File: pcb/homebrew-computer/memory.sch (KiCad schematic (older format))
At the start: 3 parts

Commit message: Add clock generation
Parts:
- removed U? (x2): SN74AVC8T245RHLR, symbol 74AVC8T245:SN74AVC8T245RHLR
- added U? (x3): SN74AVC16T245DGGR, symbol 74AVC16T245:SN74AVC16T245DGGR
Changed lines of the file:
@@
 $Descr User 9843 8268
 encoding utf-8
-Sheet 6 7
+Sheet 6 8
 Title ""
 Date ""
@@
 $EndComp
 $Comp
-L 74AVC8T245:SN74AVC8T245RHLR U?
-U 1 1 5F979582
-P 2400 1400
-F 0 "U?" H 2400 1181 50  0000 C CNN
-F 1 "SN74AVC8T245RHLR" H 2400 1090 50  0000 C CNN
-F 2 "" H 2400 1400 50  0001 C CNN
-F 3 "" H 2400 1400 50  0001 C CNN
-	1    2400 1400
+L 74AVC16T245:SN74AVC16T245DGGR U?
+U 1 1 5F907EBD
+P 2550 2800
+F 0 "U?" H 2500 2865 50  0000 C CNN
+F 1 "SN74AVC16T245DGGR" H 2500 2774 50  0000 C CNN
+F 2 "" H 2550 2800 50  0001 C CNN
+F 3 "" H 2550 2800 50  0001 C CNN
+	1    2550 2800
 	1    0    0    -1
 $EndComp
 $Comp
-L 74AVC8T245:SN74AVC8T245RHLR U?
-U 1 1 5F97A12B
-P 2400 3350
-F 0 "U?" H 2400 3131 50  0000 C CNN
-F 1 "SN74AVC8T245RHLR" H 2400 3040 50  0000 C CNN
-F 2 "" H 2400 3350 50  0001 C CNN
-F 3 "" H 2400 3350 50  0001 C CNN
-	1    2400 3350
+L 74AVC16T245:SN74AVC16T245DGGR U?
+U 2 1 5F908C70
+P 2500 3650
+F 0 "U?" H 2525 3665 50  0000 C CNN
+F 1 "SN74AVC16T245DGGR" H 2525 3574 50  0000 C CNN
+F 2 "" H 2500 3650 50  0001 C CNN
+F 3 "" H 2500 3650 50  0001 C CNN
+	2    2500 3650
 	1    0    0    -1
 $EndComp
+$Comp
+L 74AVC16T245:SN74AVC16T245DGGR U?
+U 3 1 5F909A93
+P 2550 5100
+F 0 "U?" H 2625 5115 50  0000 C CNN
+F 1 "SN74AVC16T245DGGR" H 2625 5024 50  0000 C CNN
+F 2 "" H 2550 5100 50  0001 C CNN
+F 3 "" H 2550 5100 50  0001 C CNN
+	3    2550 5100
+	1    0    0    -1
+$EndComp

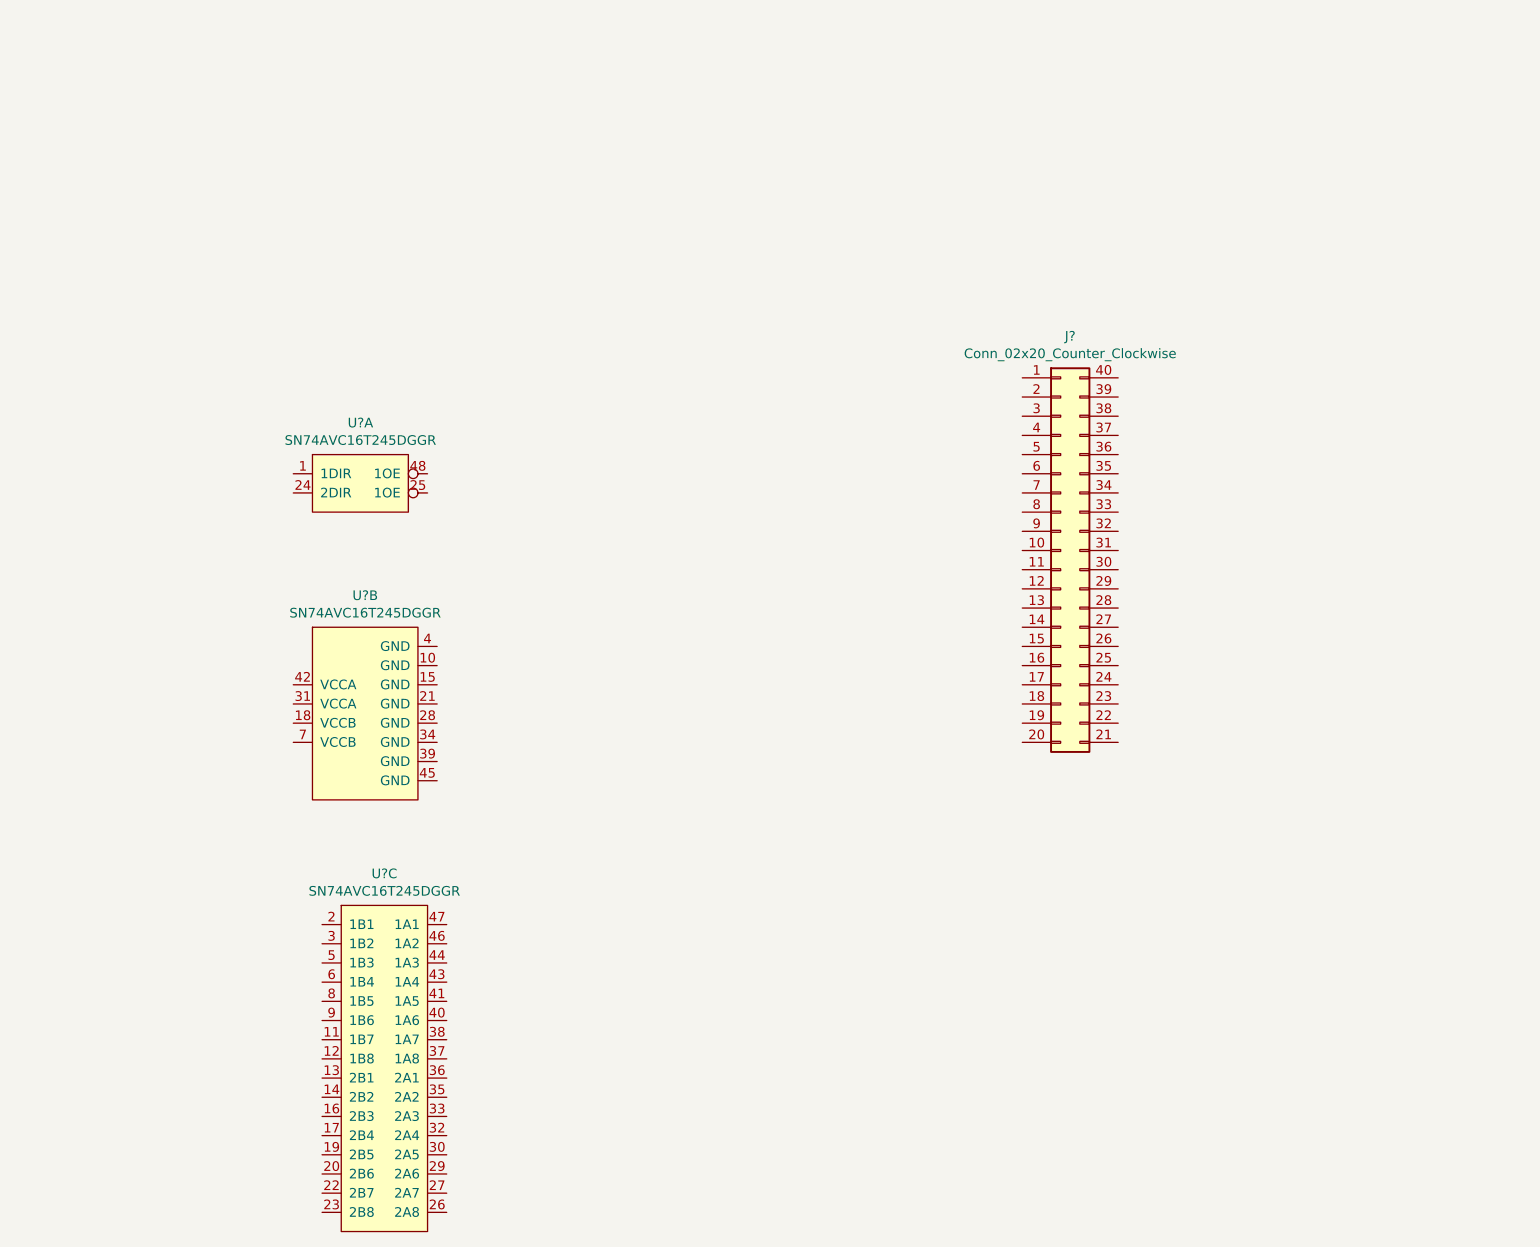
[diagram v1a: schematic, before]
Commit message: Add the memory interface logic
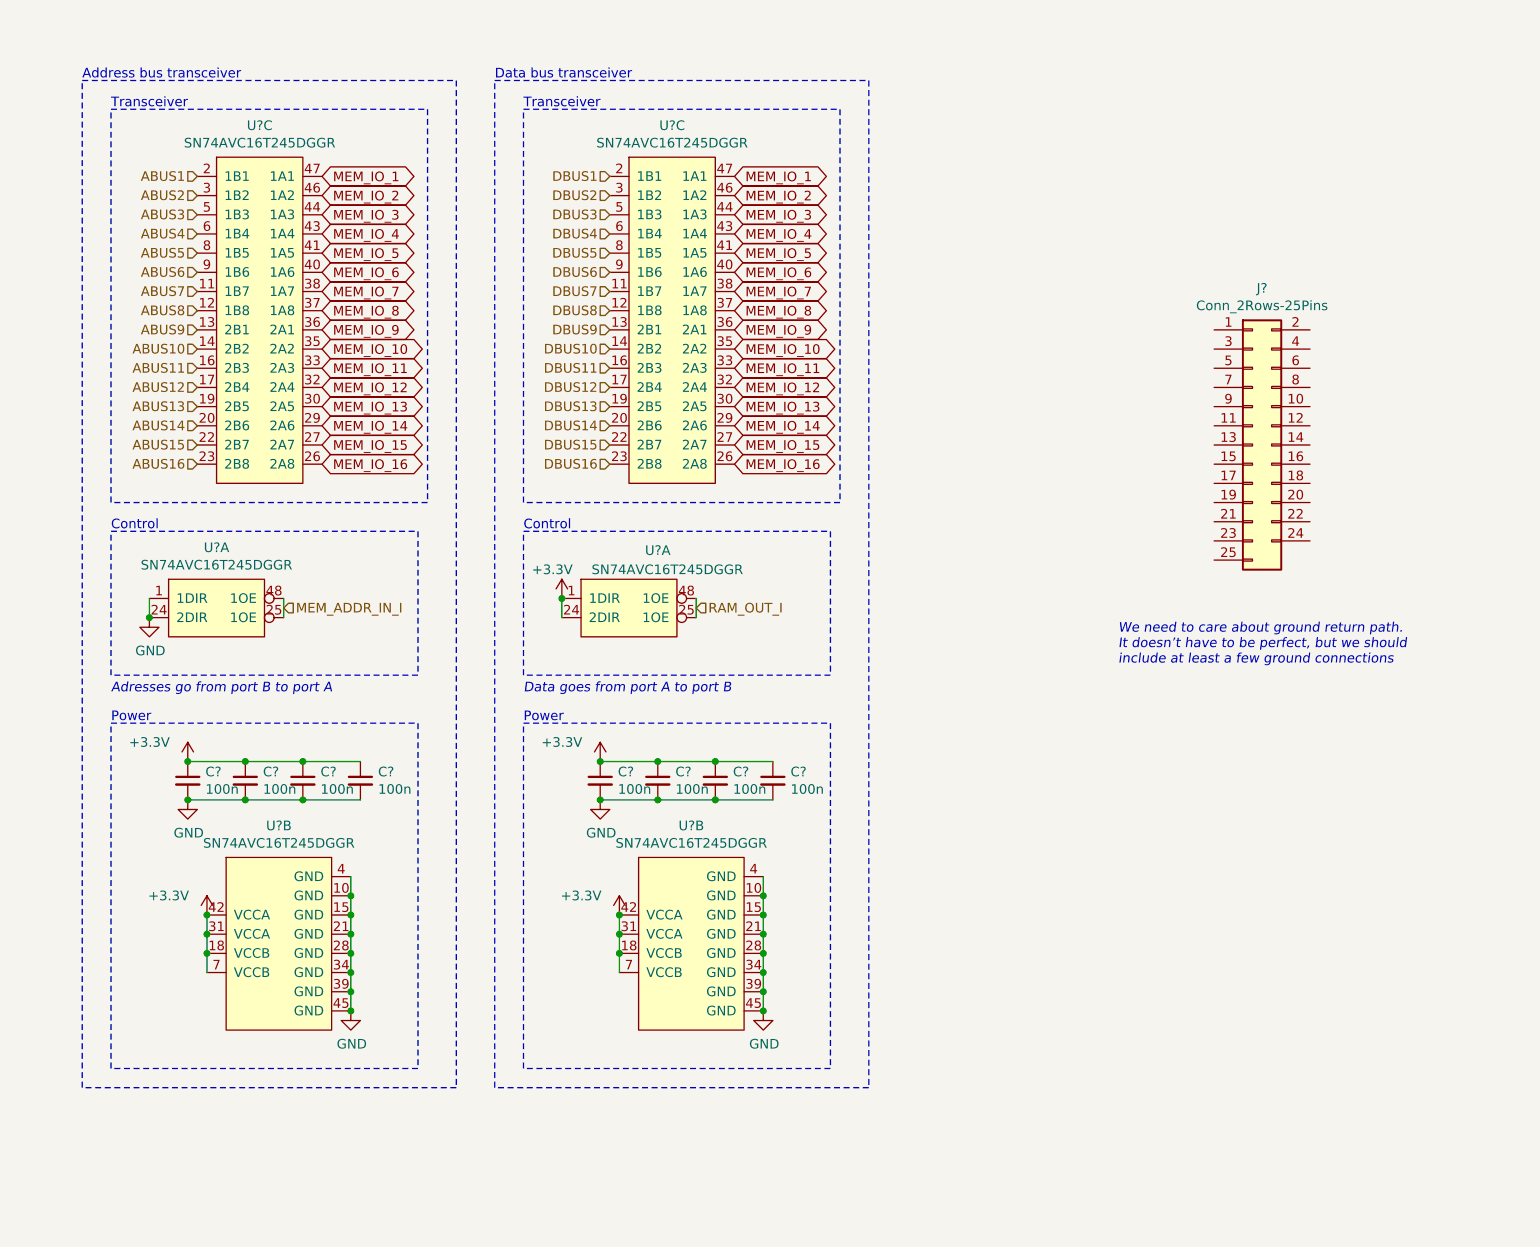
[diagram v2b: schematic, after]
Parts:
- removed J?: Conn_02x20_Counter_Clockwise, symbol Connector_Generic:Conn_02x20_Counter_Clockwise
- added C? (x8): 100n, symbol Device:C_Small
- added J?: Conn_2Rows-25Pins, symbol Connector_Generic:Conn_2Rows-25Pins
- added U? (x3): SN74AVC16T245DGGR, symbol 74AVC16T245:SN74AVC16T245DGGR
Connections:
- net GND: now reaches U?.1 (1DIR)
- net GND: now also U?.10 (GND), U?.15 (GND), U?.21 (GND), U?.24 (2DIR), U?.28 (GND), U?.34 (GND), U?.39 (GND), U?.4 (GND), U?.45 (GND), C?.2, C?.2, C?.2, C?.2, C?.2, C?.2, C?.2, C?.2, U?.10 (GND), U?.15 (GND), U?.21 (GND), U?.28 (GND), U?.34 (GND), U?.39 (GND), U?.4 (GND), U?.45 (GND)
- net MEM_ADDR_IN_I: now reaches U?.25 (1OE)
- net MEM_ADDR_IN_I: now also U?.48 (1OE)
- net +3V3: now reaches U?.18 (VCCB)
- net +3V3: now also U?.31 (VCCA), U?.42 (VCCA), U?.7 (VCCB), C?.1, C?.1, C?.1, C?.1, C?.1, C?.1, C?.1, C?.1, U?.1 (1DIR), U?.18 (VCCB), U?.24 (2DIR), U?.31 (VCCA), U?.42 (VCCA), U?.7 (VCCB)
- net ABUS7: now reaches U?.11 (1B7)
- net ABUS8: now reaches U?.12 (1B8)
- net ABUS9: now reaches U?.13 (2B1)
- net ABUS10: now reaches U?.14 (2B2)
- net ABUS11: now reaches U?.16 (2B3)
- net ABUS12: now reaches U?.17 (2B4)
- net ABUS13: now reaches U?.19 (2B5)
- net ABUS1: now reaches U?.2 (1B1)
- net ABUS14: now reaches U?.20 (2B6)
- net ABUS15: now reaches U?.22 (2B7)
- net ABUS16: now reaches U?.23 (2B8)
- net MEM_IO_16: now reaches U?.26 (2A8)
- net MEM_IO_16: now also U?.26 (2A8)
- net MEM_IO_15: now reaches U?.27 (2A7)
- net MEM_IO_15: now also U?.27 (2A7)
- net MEM_IO_14: now reaches U?.29 (2A6)
- net MEM_IO_14: now also U?.29 (2A6)
- net ABUS2: now reaches U?.3 (1B2)
- net MEM_IO_13: now reaches U?.30 (2A5)
- net MEM_IO_13: now also U?.30 (2A5)
- net MEM_IO_12: now reaches U?.32 (2A4)
- net MEM_IO_12: now also U?.32 (2A4)
- net MEM_IO_11: now reaches U?.33 (2A3)
- net MEM_IO_11: now also U?.33 (2A3)
- net MEM_IO_10: now reaches U?.35 (2A2)
- net MEM_IO_10: now also U?.35 (2A2)
- net MEM_IO_9: now reaches U?.36 (2A1)
- net MEM_IO_9: now also U?.36 (2A1)
- net MEM_IO_8: now reaches U?.37 (1A8)
- net MEM_IO_8: now also U?.37 (1A8)
- net MEM_IO_7: now reaches U?.38 (1A7)
- net MEM_IO_7: now also U?.38 (1A7)
- net MEM_IO_6: now reaches U?.40 (1A6)
- net MEM_IO_6: now also U?.40 (1A6)
- net MEM_IO_5: now reaches U?.41 (1A5)
- net MEM_IO_5: now also U?.41 (1A5)
- net MEM_IO_4: now reaches U?.43 (1A4)
- net MEM_IO_4: now also U?.43 (1A4)
- net MEM_IO_3: now reaches U?.44 (1A3)
- net MEM_IO_3: now also U?.44 (1A3)
- net MEM_IO_2: now reaches U?.46 (1A2)
- net MEM_IO_2: now also U?.46 (1A2)
- net MEM_IO_1: now reaches U?.47 (1A1)
- net MEM_IO_1: now also U?.47 (1A1)
- net ABUS3: now reaches U?.5 (1B3)
- net ABUS4: now reaches U?.6 (1B4)
- net ABUS5: now reaches U?.8 (1B5)
- net ABUS6: now reaches U?.9 (1B6)
- new net DBUS1: U?.2 (1B1)
- new net DBUS10: U?.14 (2B2)
- new net DBUS11: U?.16 (2B3)
- new net DBUS12: U?.17 (2B4)
- new net DBUS13: U?.19 (2B5)
- new net DBUS14: U?.20 (2B6)
- new net DBUS15: U?.22 (2B7)
- new net DBUS16: U?.23 (2B8)
- new net DBUS2: U?.3 (1B2)
- new net DBUS3: U?.5 (1B3)
- new net DBUS4: U?.6 (1B4)
- new net DBUS5: U?.8 (1B5)
- new net DBUS6: U?.9 (1B6)
- new net DBUS7: U?.11 (1B7)
- new net DBUS8: U?.12 (1B8)
- new net DBUS9: U?.13 (2B1)
- new net RAM_OUT_I: U?.25 (1OE), U?.48 (1OE)
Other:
- note added: "Address bus transceiver"
- note added: "Adresses go from port B to port A"
- note added: "Control"
- note added: "Data bus transceiver"
- note added: "Data goes from port A to port B"
- note added: "Power"
- note added: "Transceiver"
- note added: "We need to care about ground return path.\nIt doesn’t have to be perfect, but we should\ninclude at least a few ground connections"
- moved on the sheet: U?A, U?B, U?C

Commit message: Add beginning of peripheral ios
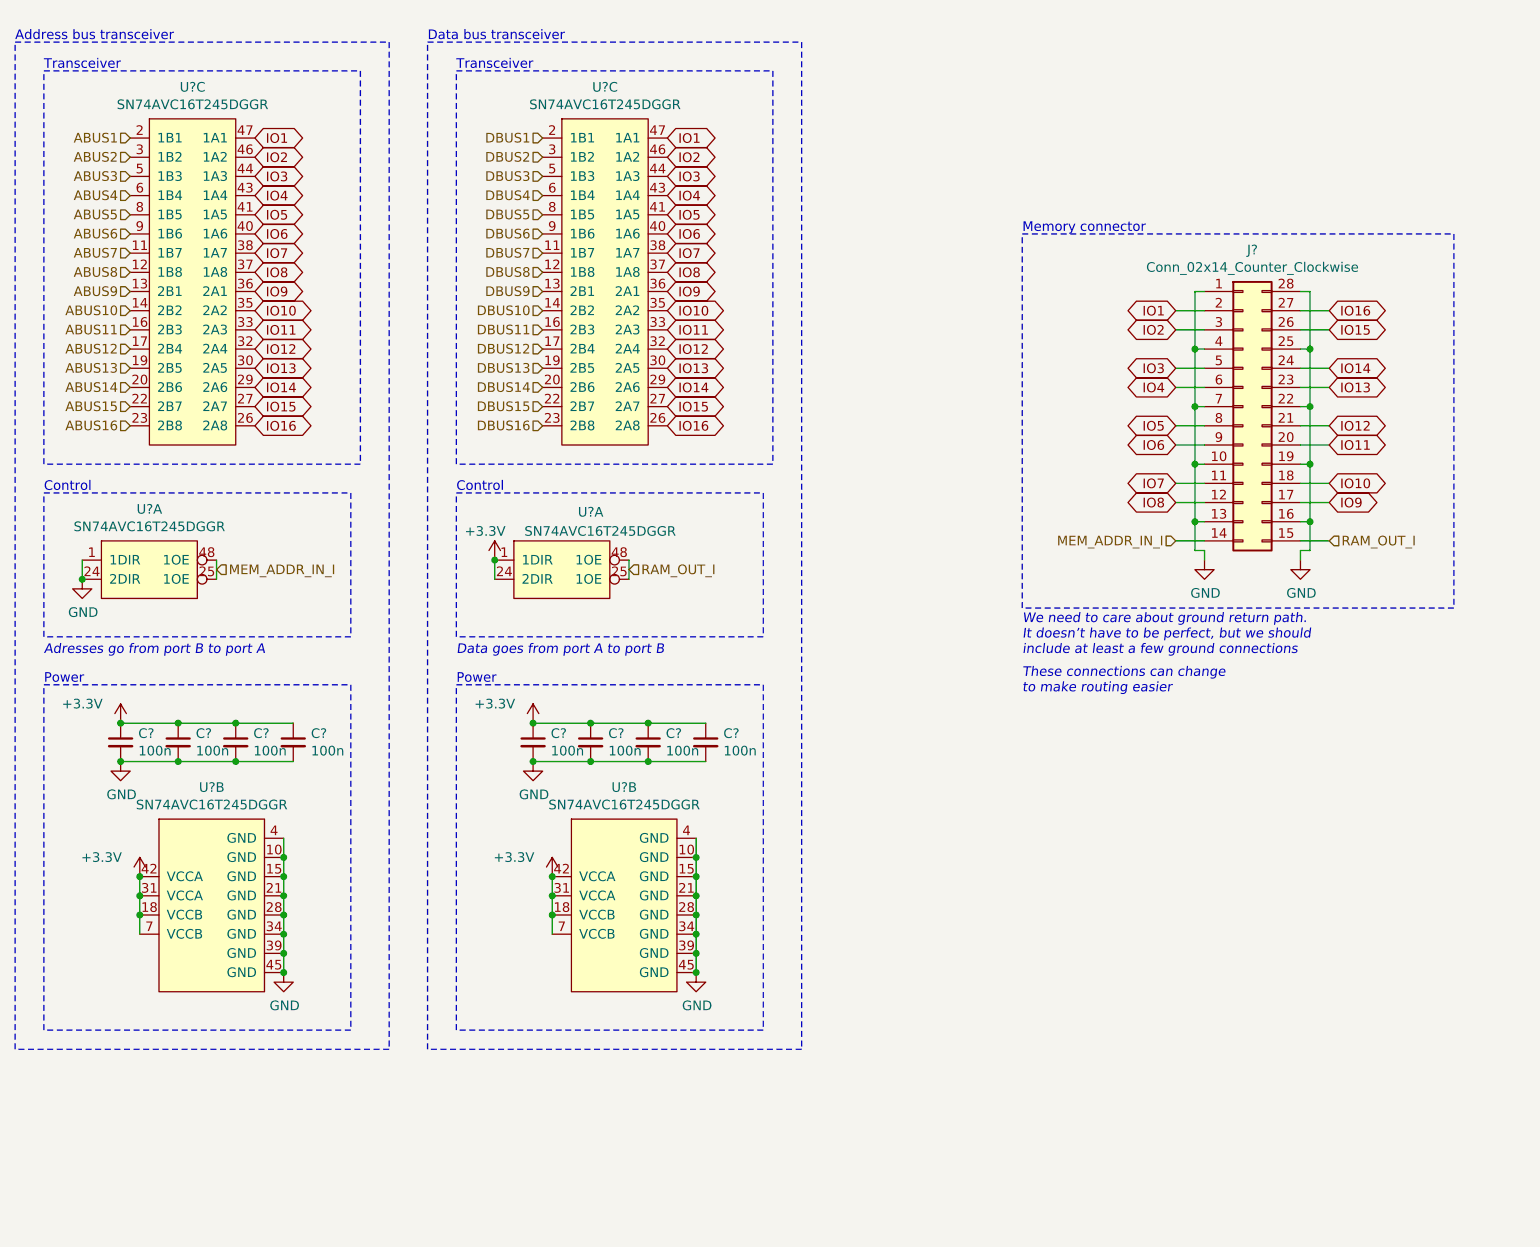
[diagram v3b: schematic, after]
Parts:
- removed J?: Conn_2Rows-25Pins, symbol Connector_Generic:Conn_2Rows-25Pins
- added J?: Conn_02x14_Counter_Clockwise, symbol Connector_Generic:Conn_02x14_Counter_Clockwise
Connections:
- net GND: now also J?.1 (Pin_1), J?.10 (Pin_10), J?.13 (Pin_13), J?.16 (Pin_16), J?.19 (Pin_19), J?.22 (Pin_22), J?.25 (Pin_25), J?.28 (Pin_28), J?.4 (Pin_4), J?.7 (Pin_7)
- net MEM_ADDR_IN_I: now also J?.14 (Pin_14)
- net RAM_OUT_I: now also J?.15 (Pin_15)
- net MEM_IO_1 renamed IO1
- net IO1: now also J?.2 (Pin_2)
- net MEM_IO_10 renamed IO10
- net IO10: now also J?.18 (Pin_18)
- net MEM_IO_11 renamed IO11
- net IO11: now also J?.20 (Pin_20)
- net MEM_IO_12 renamed IO12
- net IO12: now also J?.21 (Pin_21)
- net MEM_IO_13 renamed IO13
- net IO13: now also J?.23 (Pin_23)
- net MEM_IO_14 renamed IO14
- net IO14: now also J?.24 (Pin_24)
- net MEM_IO_15 renamed IO15
- net IO15: now also J?.26 (Pin_26)
- net MEM_IO_16 renamed IO16
- net IO16: now also J?.27 (Pin_27)
- net MEM_IO_2 renamed IO2
- net IO2: now also J?.3 (Pin_3)
- net MEM_IO_3 renamed IO3
- net IO3: now also J?.5 (Pin_5)
- net MEM_IO_4 renamed IO4
- net IO4: now also J?.6 (Pin_6)
- net MEM_IO_5 renamed IO5
- net IO5: now also J?.8 (Pin_8)
- net MEM_IO_6 renamed IO6
- net IO6: now also J?.9 (Pin_9)
- net MEM_IO_7 renamed IO7
- net IO7: now also J?.11 (Pin_11)
- net MEM_IO_8 renamed IO8
- net IO8: now also J?.12 (Pin_12)
- net MEM_IO_9 renamed IO9
- net IO9: now also J?.17 (Pin_17)
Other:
- note added: "Memory connector"
- note added: "These connections can change\nto make routing easier"
- moved on the sheet: C?, U?A, U?B, U?C

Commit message: Keep working on the peripheral interface
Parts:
- removed J?: Conn_02x14_Counter_Clockwise, symbol Connector_Generic:Conn_02x14_Counter_Clockwise
- added D? (x4): D_Small, symbol Device:D_Small
- added J?: Conn_02x20_Counter_Clockwise, symbol Connector_Generic:Conn_02x20_Counter_Clockwise
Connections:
- net GND: now also J?.1 (Pin_1), J?.10 (Pin_10), J?.13 (Pin_13), J?.15 (Pin_15), J?.16 (Pin_16), J?.17 (Pin_17), J?.18 (Pin_18), J?.19 (Pin_19), J?.20 (Pin_20), J?.21 (Pin_21), J?.22 (Pin_22), J?.25 (Pin_25), J?.28 (Pin_28), J?.31 (Pin_31), J?.34 (Pin_34), J?.37 (Pin_37), J?.4 (Pin_4), J?.40 (Pin_40), J?.7 (Pin_7)
- net IO1: now also J?.2 (Pin_2)
- net IO10: now also J?.30 (Pin_30)
- net IO11: now also J?.32 (Pin_32)
- net IO12: now also J?.33 (Pin_33)
- net IO13: now also J?.35 (Pin_35)
- net IO14: now also J?.36 (Pin_36)
- net IO15: now also J?.38 (Pin_38)
- net IO16: now also J?.39 (Pin_39)
- net IO2: now also J?.3 (Pin_3)
- net IO3: now also J?.5 (Pin_5)
- net IO4: now also J?.6 (Pin_6)
- net IO5: now also J?.8 (Pin_8)
- net IO6: now also J?.9 (Pin_9)
- net IO7: now also J?.11 (Pin_11)
- net IO8: now also J?.12 (Pin_12)
- net IO9: now also J?.29 (Pin_29)
- net RAM_OUT_I: now also D?.2 (A), J?.27 (Pin_27); no longer U?.25 (1OE), U?.48 (1OE)
- net MEM_ADDR_IN_I renamed RAM_ADDR_IN_I
- net RAM_ADDR_IN_I: now also J?.14 (Pin_14)
- new net: D?.1 (K), D?.1 (K), D?.1 (K), D?.1 (K), U?.25 (1OE), U?.48 (1OE)
- new net RAM_INB_I: D?.2 (A), J?.23 (Pin_23)
- new net RAM_IN_I: D?.2 (A), J?.26 (Pin_26)
- new net RAM_OUTB_I: D?.2 (A), J?.24 (Pin_24)
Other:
- note added: "Data goes from port A to port B\nWe use diodes to implement the OR\nfunction as there will only be one \nactive at the same time"
- note removed: "Data goes from port A to port B"
- moved on the sheet: C?, U?A, U?B, U?C

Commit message: Remove the address bus as it would require too big of a connector
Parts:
- removed C? (x4): 100n, symbol Device:C_Small
- removed U? (x3): SN74AVC16T245DGGR, symbol 74AVC16T245:SN74AVC16T245DGGR
- added D?: D_Small, symbol Device:D_Small
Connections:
- net RAM_ADDR_IN_I: now also D?.2 (A)
- net at D?.1 (K), D?.1 (K), D?.1 (K)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: now also D?.1 (K)
- net DBUS1 renamed BUS1
- net DBUS10 renamed BUS10
- net DBUS11 renamed BUS11
- net DBUS12 renamed BUS12
- net DBUS13 renamed BUS13
- net DBUS14 renamed BUS14
- net DBUS15 renamed BUS15
- net DBUS16 renamed BUS16
- net DBUS2 renamed BUS2
- net DBUS3 renamed BUS3
- net DBUS4 renamed BUS4
- net DBUS5 renamed BUS5
- net DBUS6 renamed BUS6
- net DBUS7 renamed BUS7
- net DBUS8 renamed BUS8
- net DBUS9 renamed BUS9
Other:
- note added: "Bus transceiver"
- note removed: "Address bus transceiver"
- note removed: "Adresses go from port B to port A"
- note removed: "Data bus transceiver"
- moved on the sheet: C?, D?, J?, U?A, U?B, U?C
